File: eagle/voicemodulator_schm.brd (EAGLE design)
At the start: 109 x 84 mm, 42 parts, among them T1 2N5089, T2 2N5089, T3 2N5089, T4 2N5089

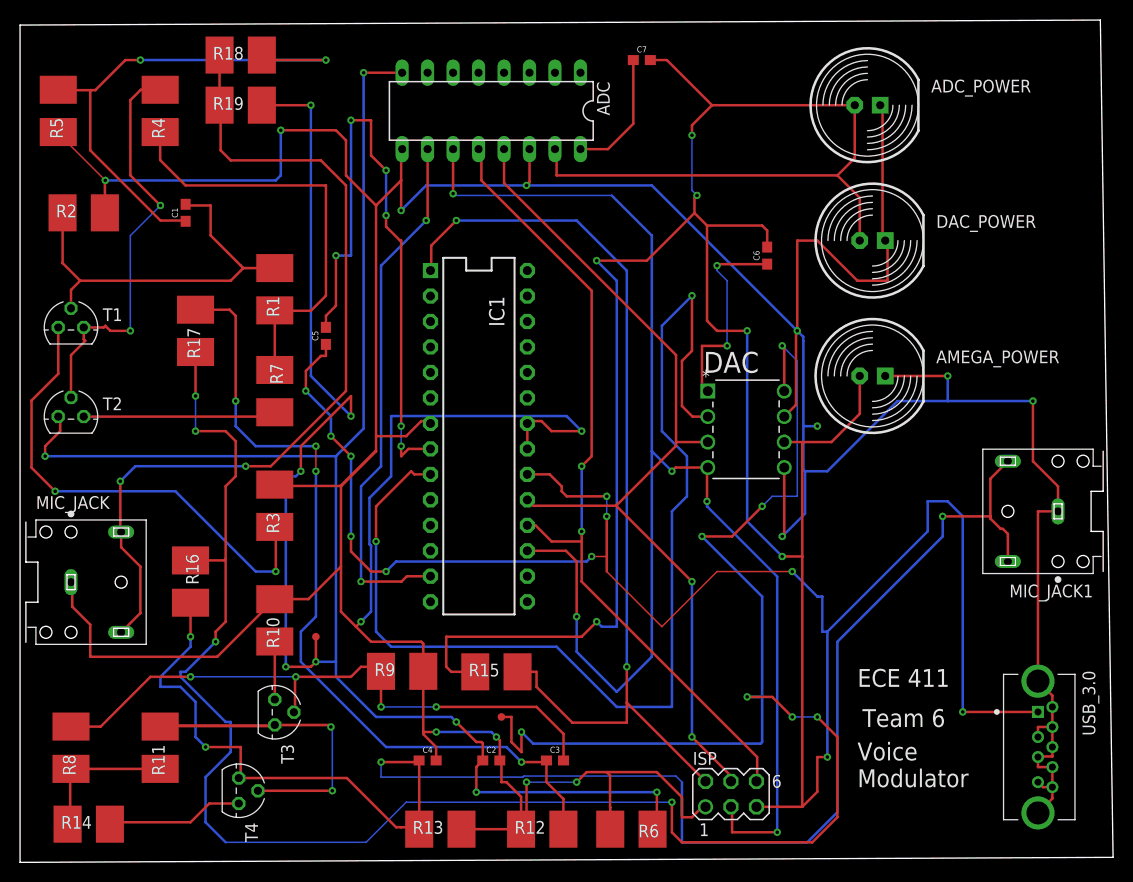
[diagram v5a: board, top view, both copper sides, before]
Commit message: Add caps for input voltage coming in through USB 3.0, remaining wire widths resolved.
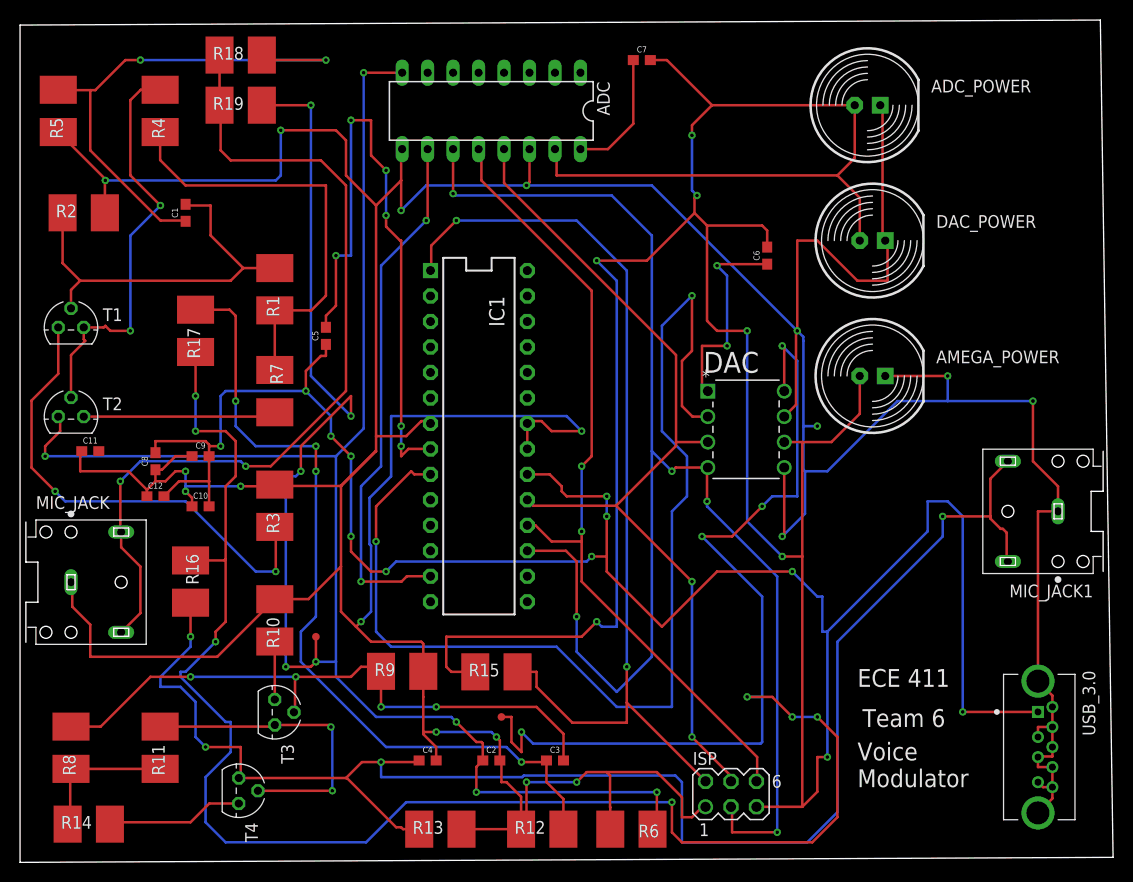
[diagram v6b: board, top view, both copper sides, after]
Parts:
- added C10, C11, C12, C8, C9: 10nF, SparkFun-Capacitors:0603
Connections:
- net GND: now also C10.1, C11.1, C12.1, C8.1, C9.1
- net VCC: now also C10.2, C12.2, C8.2, C9.2
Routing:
- net GND: track 495.8 -> 528.7 mm, vias 15 -> 18
- net VCC: track 421.5 -> 454.2 mm, vias 17 -> 18
- net N$14: track 48.3 -> 31.0 mm
- net N$11: track 166.7 -> 158.9 mm
- net N$15: track 16.2 -> 14.7 mm

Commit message: Ground plane and multiple vias added for flooded ground
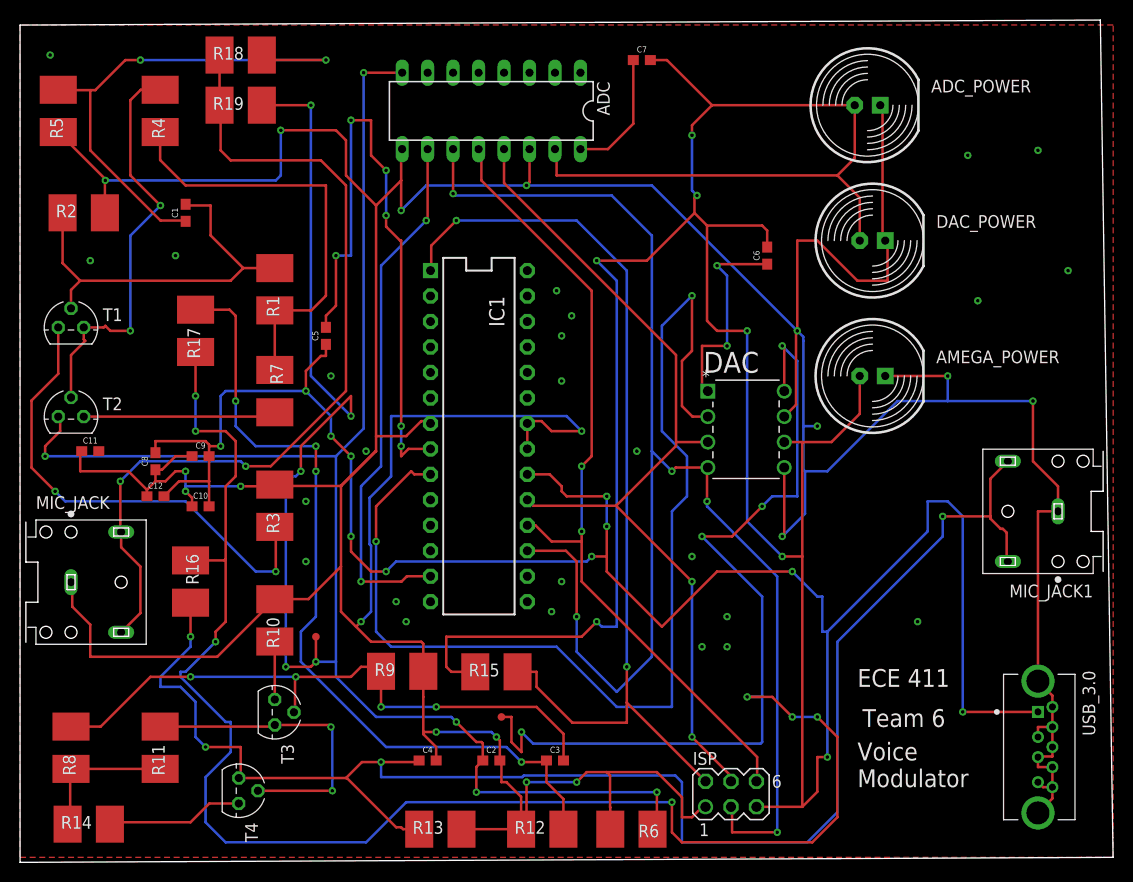
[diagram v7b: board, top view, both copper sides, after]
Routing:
- net GND: vias 18 -> 42
- added copper zone on layer 1, net GND
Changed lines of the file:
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@@
 <wire x1="78.106771875" y1="52.00150625" x2="78.106771875" y2="43.5" width="0.254" layer="16"/>
 <wire x1="40.2082" y1="19.05" x2="40.2082" y2="18" width="0.254" layer="1"/>
+<polygon width="0.254" layer="1">
+<vertex x="0" y="83.5"/>
+<vertex x="0" y="0.5"/>
+<vertex x="109" y="0.5"/>
+<vertex x="109" y="83.5"/>
+</polygon>
+<via x="94.5" y="70.5" extent="1-16" drill="0.35"/>
+<via x="15.5" y="60.5" extent="1-16" drill="0.35"/>
+<via x="7" y="60" extent="1-16" drill="0.35"/>
+<via x="70.5" y="21.5" extent="1-16" drill="0.35"/>
+<via x="95.5" y="56" extent="1-16" drill="0.35"/>
+<via x="104.5" y="59" extent="1-16" drill="0.35"/>
+<via x="101.5" y="71" extent="1-16" drill="0.35"/>
+<via x="89.5" y="24" extent="1-16" drill="0.35"/>
+<via x="70.5" y="24.5" extent="1-16" drill="0.35"/>
+<via x="67" y="30.5" extent="1-16" drill="0.35"/>
+<via x="61.5" y="41" extent="1-16" drill="0.35"/>
+<via x="54" y="52.5" extent="1-16" drill="0.35"/>
+<via x="54" y="48" extent="1-16" drill="0.35"/>
+<via x="53.5" y="57" extent="1-16" drill="0.35"/>
+<via x="55" y="54.5" extent="1-16" drill="0.35"/>
+<via x="31" y="48.5" extent="1-16" drill="0.35"/>
+<via x="34.5" y="41" extent="1-16" drill="0.35"/>
+<via x="28.5" y="36" extent="1-16" drill="0.35"/>
+<via x="28.5" y="30" extent="1-16" drill="0.35"/>
+<via x="38.5" y="24" extent="1-16" drill="0.35"/>
+<via x="53" y="25" extent="1-16" drill="0.35"/>
+<via x="68" y="21.5" extent="1-16" drill="0.35"/>
+<via x="54" y="28" extent="1-16" drill="0.35"/>
+<via x="37.5" y="26" extent="1-16" drill="0.35"/>
 </signal>
 <signal name="N$1">
@@
 <contactref element="C5" pad="1"/>
 <via x="77" y="29" extent="1-16" drill="0.35"/>
-<via x="58.5" y="34.5" extent="1-16" drill="0.35"/>
+<via x="58.5" y="33.5" extent="1-16" drill="0.35"/>
 <via x="58.5" y="36.5" extent="1-16" drill="0.35"/>
 <via x="36.5" y="29" extent="1-16" drill="0.35"/>
@@
 <wire x1="67.25" y1="66.25" x2="67.25" y2="64.75" width="0.254" layer="1"/>
 <wire x1="73.43" y1="5.54" x2="78" y2="5.54" width="0.254" layer="1"/>
-<wire x1="58.5" y1="30.5" x2="58.5" y2="34.5" width="0.254" layer="1"/>
+<wire x1="58.5" y1="33.5" x2="58.5" y2="30.5" width="0.254" layer="1"/>
 <wire x1="67.5" y1="66.5" x2="67.25" y2="66.25" width="0.254" layer="1"/>
 <wire x1="57.5" y1="24" x2="58" y2="23.5" width="0.254" layer="16"/>
@@
 <wire x1="67.5" y1="66.5" x2="67" y2="67" width="0.254" layer="16"/>
 <wire x1="67" y1="67" x2="67" y2="72.5" width="0.254" layer="16"/>
-<wire x1="58.5" y1="34.5" x2="58.5" y2="36.5" width="0.254" layer="16"/>
+<wire x1="58.5" y1="36.5" x2="58.5" y2="33.5" width="0.254" layer="16"/>
 </signal>
 <signal name="N$2">
@@
 <wire x1="61.15" y1="80" x2="61.15" y2="73.65" width="0.254" layer="1"/>
 </signal>
+<signal name="N$26">
+<via x="3" y="80.5" extent="1-16" drill="0.35"/>
+</signal>
 </signals>
